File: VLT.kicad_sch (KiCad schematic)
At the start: 65 parts, among them J1 TFT, J2 DEBUG, Q1 AO3401A, Q2 BSS138, Q3 AO3401A, U1 AP2112K-3.3, U2 W25Q128JVS, U3 RP2350B-QFN80, Y1 12MHz

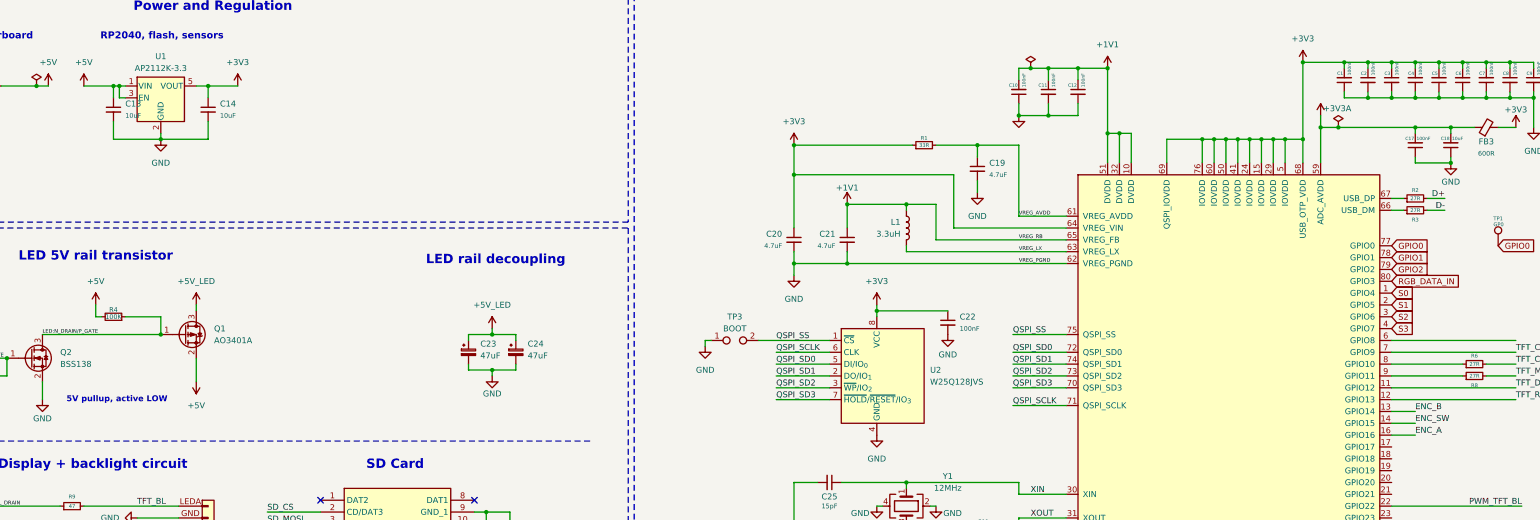
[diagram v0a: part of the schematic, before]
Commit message: Changed encoder pinout A: GP16>GP15, B: GP14>GP15, SW: GP15>GP16
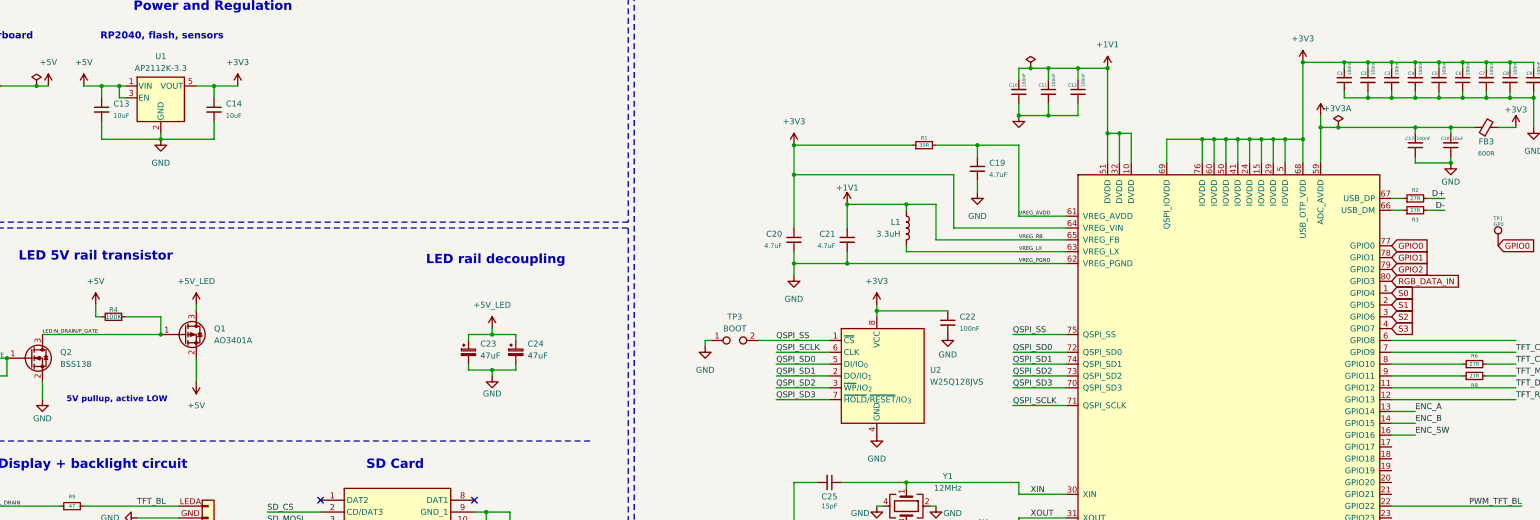
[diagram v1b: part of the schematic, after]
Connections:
- net ENC_A: now also U3.13 (GPIO14); no longer U3.16 (GPIO16)
- net ENC_B: now also U3.14 (GPIO15); no longer U3.13 (GPIO14)
- net ENC_SW: now also U3.16 (GPIO16); no longer U3.14 (GPIO15)
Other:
- moved on the sheet: C13, C14
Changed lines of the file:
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@@
 	)
 	(junction
+		(at 77.47 36.83)
+		(diameter 0)
+		(color 0 0 0 0)
+	)
+	(junction
 		(at 57.15 95.25)
 		(diameter 0)
@@
 	)
 	(junction
-		(at 80.01 36.83)
-		(diameter 0)
-		(color 0 0 0 0)
-	)
-	(junction
 		(at 90.17 48.26)
 		(diameter 0)
@@
 	)
 	(junction
-		(at 384.81 39.37)
+		(at 101.6 36.83)
 		(diameter 0)
 		(color 0 0 0 0)
 	)
 	(junction
-		(at 100.33 36.83)
+		(at 384.81 39.37)
 		(diameter 0)
 		(color 0 0 0 0)
@@
 	(wire
 		(pts
-			(xy 73.66 36.83) (xy 80.01 36.83)
+			(xy 73.66 36.83) (xy 77.47 36.83)
 		)
 		(stroke
@@
 	(wire
 		(pts
+			(xy 77.47 36.83) (xy 81.28 36.83)
+		)
+		(stroke
+			(width 0)
+			(type default)
+		)
+	)
+	(wire
+		(pts
 			(xy 102.87 252.73) (xy 102.87 254)
 		)
@@
 	(wire
 		(pts
-			(xy 100.33 44.45) (xy 100.33 48.26)
+			(xy 101.6 44.45) (xy 101.6 48.26)
 		)
 		(stroke
@@
 	(wire
 		(pts
-			(xy 80.01 44.45) (xy 80.01 48.26)
+			(xy 77.47 44.45) (xy 77.47 48.26)
 		)
 		(stroke
@@
 	(wire
 		(pts
-			(xy 80.01 48.26) (xy 90.17 48.26)
+			(xy 77.47 48.26) (xy 90.17 48.26)
 		)
 		(stroke
@@
 	(wire
 		(pts
-			(xy 97.79 36.83) (xy 100.33 36.83)
+			(xy 97.79 36.83) (xy 101.6 36.83)
 		)
 		(stroke
@@
 	(wire
 		(pts
-			(xy 100.33 48.26) (xy 90.17 48.26)
+			(xy 101.6 48.26) (xy 90.17 48.26)
 		)
 		(stroke
@@
 	(wire
 		(pts
-			(xy 80.01 36.83) (xy 81.28 36.83)
-		)
-		(stroke
-			(width 0)
-			(type default)
-		)
-	)
-	(wire
-		(pts
 			(xy 73.66 127) (xy 93.98 127)
 		)
@@
 	(wire
 		(pts
-			(xy 80.01 39.37) (xy 80.01 36.83)
+			(xy 77.47 39.37) (xy 77.47 36.83)
 		)
 		(stroke
@@
 	(wire
 		(pts
-			(xy 100.33 36.83) (xy 106.68 36.83)
-		)
-		(stroke
-			(width 0)
-			(type default)
-		)
-	)
-	(wire
-		(pts
 			(xy 313.69 48.26) (xy 316.23 48.26)
 		)
@@
 	(wire
 		(pts
-			(xy 100.33 39.37) (xy 100.33 36.83)
+			(xy 101.6 39.37) (xy 101.6 36.83)
 		)
 		(stroke
@@
 	(wire
 		(pts
+			(xy 101.6 36.83) (xy 106.68 36.83)
+		)
+		(stroke
+			(width 0)
+			(type default)
+		)
+	)
+	(wire
+		(pts
 			(xy 85.09 144.78) (xy 93.98 144.78)
 		)
@@
 	)
 	(label "ENC_SW"
-		(at 359.41 109.22 0)
+		(at 359.41 111.76 0)
 		(effects
 			(font
@@
 	)
 	(label "ENC_B"
-		(at 359.41 106.68 0)
+		(at 359.41 109.22 0)
 		(effects
 			(font
@@
 	)
 	(label "ENC_A"
-		(at 359.41 111.76 0)
+		(at 359.41 106.68 0)
 		(effects
 			(font
@@
 	(symbol
 		(lib_id "Mars_Library:Capacitor_0603_10uF")
-		(at 80.01 41.91 0)
+		(at 77.47 41.91 0)
 		(unit 1)
 		(exclude_from_sim no)
@@
 		(fields_autoplaced yes)
 		(property "Reference" "C13"
-			(at 82.55 40.6462 0)
+			(at 80.01 40.6462 0)
 			(effects
 				(font
@@
 		)
 		(property "Value" "10uF"
-			(at 82.55 43.1863 0)
+			(at 80.01 43.1863 0)
 			(effects
 				(font
@@
 		)
 		(property "Footprint" "Mars_Library:C_0603"
-			(at 80.01 41.91 0)
+			(at 77.47 41.91 0)
 			(effects
 				(font
@@
 		)
 		(property "Datasheet" "~"
-			(at 80.01 41.91 0)
+			(at 77.47 41.91 0)
 			(effects
 				(font
@@
 		)
 		(property "Description" "Unpolarized capacitor, small symbol"
-			(at 80.01 41.91 0)
+			(at 77.47 41.91 0)
 			(effects
 				(font
@@
 		)
 		(property "LCSC" "C19702"
-			(at 80.01 41.91 0)
+			(at 77.47 41.91 0)
 			(effects
 				(font
@@
 	(symbol
 		(lib_id "Mars_Library:Capacitor_0603_10uF")
-		(at 100.33 41.91 0)
+		(at 101.6 41.91 0)
 		(unit 1)
 		(exclude_from_sim no)
@@
 		(fields_autoplaced yes)
 		(property "Reference" "C14"
-			(at 102.87 40.6462 0)
+			(at 104.14 40.6462 0)
 			(effects
 				(font
@@
 		)
 		(property "Value" "10uF"
-			(at 102.87 43.1863 0)
+			(at 104.14 43.1863 0)
 			(effects
 				(font
@@
 		)
 		(property "Footprint" "Mars_Library:C_0603"
-			(at 100.33 41.91 0)
+			(at 101.6 41.91 0)
 			(effects
 				(font
@@
 		)
 		(property "Datasheet" "~"
-			(at 100.33 41.91 0)
+			(at 101.6 41.91 0)
 			(effects
 				(font
@@
 		)
 		(property "Description" "Unpolarized capacitor, small symbol"
-			(at 100.33 41.91 0)
+			(at 101.6 41.91 0)
 			(effects
 				(font
@@
 		)
 		(property "LCSC" "C19702"
-			(at 100.33 41.91 0)
+			(at 101.6 41.91 0)
 			(effects
 				(font

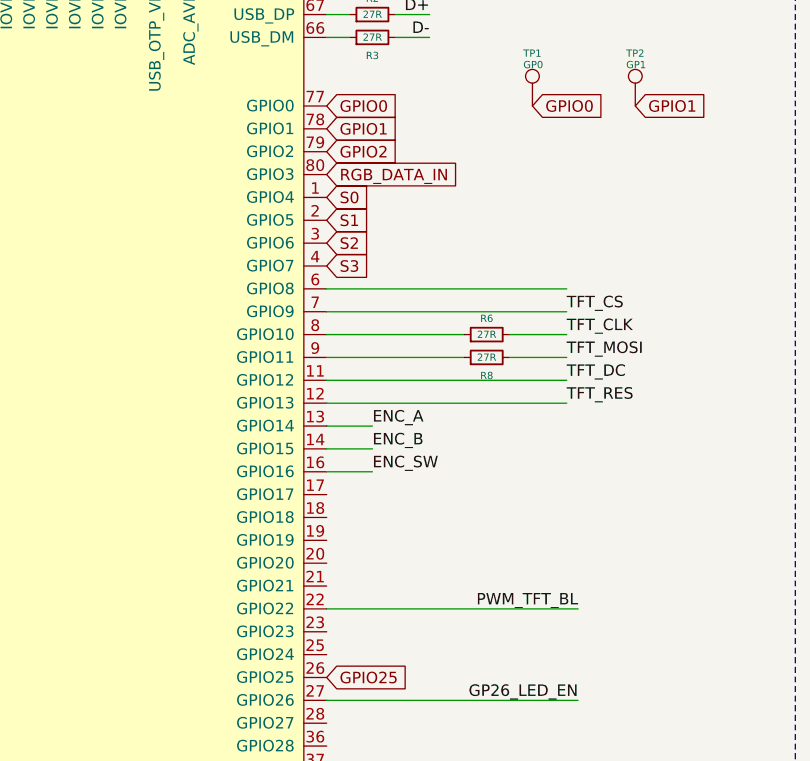
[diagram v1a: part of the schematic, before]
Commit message: Changed WS2812B pin. RGB_DATA_IN: GP3>GP21
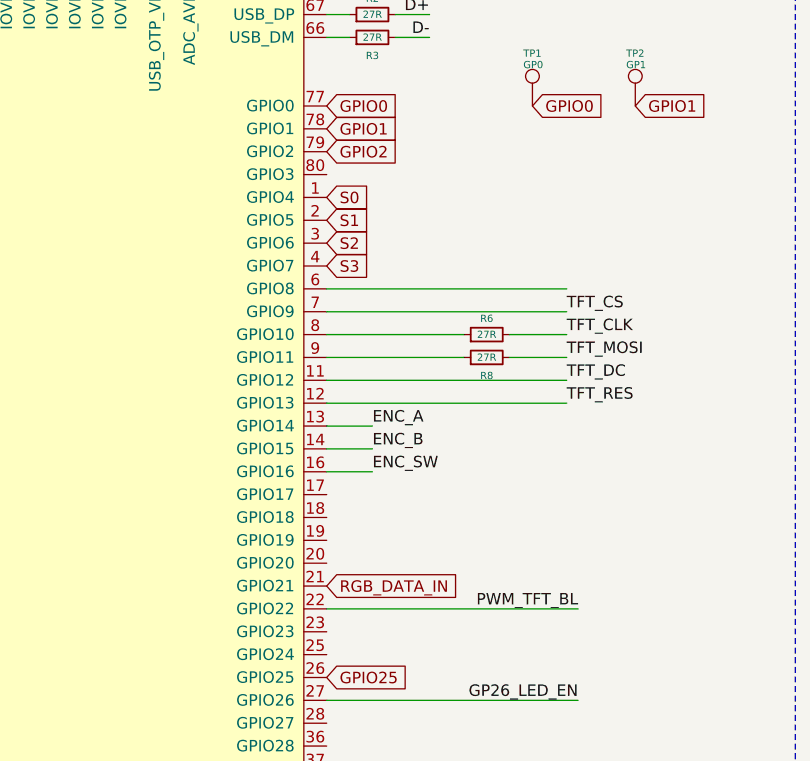
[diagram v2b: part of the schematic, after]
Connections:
- net RGB_DATA_IN: now also U3.21 (GPIO21); no longer U3.80 (GPIO3)
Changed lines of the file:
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@@
+		)
+	)
+	(global_label "RGB_DATA_IN"
+		(shape input)
+		(at 354.33 124.46 0)
+		(fields_autoplaced yes)
+		(effects
+			(font
+				(size 1.27 1.27)
+			)
+			(justify left)
+		)
+		(property "Intersheetrefs" "${INTERSHEET_REFS}"
+			(at 354.33 124.46 0)
+			(effects
+				(font
+					(size 1.27 1.27)
+				)
+				(hide yes)
+			)
 		)
 	)
@@
 				(hide yes)
 			)
-		)
-	)
-	(global_label "RGB_DATA_IN"
-		(shape input)
-		(at 354.33 78.74 0)
-		(fields_autoplaced yes)
-		(effects
-			(font
-				(size 1.27 1.27)
-			)
-			(justify left)
-		)
-		(property "Intersheetrefs" "${INTERSHEET_REFS}"
-			(at 354.33 78.74 0)
-			(effects
-				(font
-					(size 1.27 1.27)
-				)
-				(hide yes)
-			)

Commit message: Remapped pins, added MPR121
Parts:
- added C15, C16: 100nF, Mars_Library:C_0603, symbol Mars_Library:Capacitor_C_0603_100nF_0.1uF
- added R22: 75K, Mars_Library:R_0603, symbol Mars_Library:Resistor_R_0603
- added U4: MPR121QR2, Package_DFN_QFN:UQFN-20_3x3mm_P0.4mm, symbol Sensor_Touch:MPR121QR2
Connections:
- net +3V3: now also C15.1, U4.20 (VDD)
- net GND: now also C15.2, C16.2, R22.2, U4.4 (ADDR), U4.6 (VSS)
- net PWM_TFT_BL: now also U3.48 (GPIO39); no longer U3.22 (GPIO22)
- net MPR_SCL: now reaches U3.23 (GPIO23)
- net MPR_SCL: now also U4.2 (SCL)
- net MPR_IRQ: now reaches U3.25 (GPIO24)
- net MPR_IRQ: now also U4.1 (~{IRQ})
- new net: R22.1, U4.7 (REXT)
- new net: C16.1, U4.5 (VREG)
- new net ELE0: U4.8 (ELE0)
- new net ELE1: U4.9 (ELE1)
- new net ELE10: U4.18 (LED6/ELE10)
- new net ELE11: U4.19 (LED7/ELE11)
- new net ELE2: U4.10 (ELE2)
- new net ELE3: U4.11 (ELE3)
- new net ELE4: U4.12 (LED0/ELE4)
- new net ELE5: U4.13 (LED1/ELE5)
- new net ELE6: U4.14 (LED2/ELE6)
- new net ELE7: U4.15 (LED3/ELE7)
- new net ELE8: U4.16 (LED4/ELE8)
- new net ELE9: U4.17 (LED5/ELE9)
- new net MPR_SDA: U3.22 (GPIO22), U4.3 (SDA)
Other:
- moved on the sheet: ENC2

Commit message: Rev 2: Major PCB rework — haptic motor, MicroSD, NTC, CTP, split spacebar
- Added ERM haptic motor with BSS138 MOSFET driver on GP21
- Added MicroSD card slot (MSD-1-A, push-in/auto-eject)
- Added NTC thermistor with voltage divider
- Added 4-pin 0.5mm FPC connector for capacitive touch panel
- Added ferrite beads (0603 600R, 0805) for power filtering
- Added 1N4148WT protection diode and test point
- Split spacebar support: HE45 alternate 1.75u stabilizer footprint
- Full PCB re-route with 4-layer switch footprints
- All 81 hall sensors relabeled with key names in schematic
- Relaxed DRC (text height, via diameter), new via size 0.6/0.2
- Added CHANGELOG.md and wiring.cpp MUX mapping reference
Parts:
- removed R14: 10K, Mars_Library:R_0402, symbol Mars_Library:R_0603
- removed TP3: BOOT, TestPoint:TestPoint_2Pads_Pitch2.54mm_Drill0.8mm, symbol Connector:TestPoint_2Pole
- added C28: 100nF, Mars_Library:C_0603, symbol Mars_Library:Capacitor_C_0603_100nF_0.1uF
- added D1: 1N4148WT, Diode_SMD:D_SOD-523, symbol Diode:1N4148WT
- added ERM1: Motor_DC, Mars_Library:Coin_Motor_ERM_10mm, symbol Motor:Motor_DC
- added J3: FPC_4P_0.5mm, Mars_Library:XUNPU_FPC-05F-4PH20_1x4-1MP_P0.5mm, symbol Mars_Library:FPC_4P_0.5mm
- added Q4: BSS138, PCM_4ms_Package_SOT:SOT-23, symbol Mars_Transistor:BSS138
- added R14: 10K, Mars_Library:R_0402, symbol Mars_Library:Resistor_R_0402_10K
- added R23, R24: 2.2K, Mars_Library:R_0402, symbol Mars_Library:Resistor_R_0402
- added R25: 1K, Mars_Library:R_0402, symbol Mars_Library:Resistor_R_0402_1K
- added R26, R27, R28, R29: 10K, Mars_Library:R_0603, symbol Mars_Library:Resistor_R_0603_10K
- added SW1: SW_Push_Momentary, Mars_Library:SW_2x3x0.65mm_SPST_Tiny, symbol Mars_Library:SW_Push_Momentary
- added TH1: DNP (10K), Mars_Library:R_0603, symbol Device:Thermistor_NTC
- added TP3: BOOT, Mars_Library:TestPoint_Pad_D1.0mm_Minimal, symbol PCM_4ms_Connector:TestPoint
- J1: footprint Mars_Library:TFT_FPC_8P_0.5mm -> Mars_Library:XUNPU_FPC-05F-8PH20_1x8-1MP_P0.5mm
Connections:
- net +3V3: now also J1.7 (VDD), C28.1, D1.1 (K), ERM1.1 (+), R23.2, R24.2, R26.1, R27.1, R28.1, R29.1; no longer J1.VDD (Pin_7)
- net ELE2: now also J3.1 (Pin_1)
- net ELE4: now also J3.2 (Pin_2)
- net ELE6: now also J3.3 (Pin_3)
- net ELE8: now also J3.4 (Pin_4)
- net ENC_A: now also U3.39 (GPIO31), R26.2; no longer U3.13 (GPIO14)
- net ENC_B: now also U3.38 (GPIO30), R27.2; no longer U3.14 (GPIO15)
- net ENC_SW: now also U3.40 (GPIO32), R28.2; no longer U3.16 (GPIO16)
- net GND: now also J1.2 (GND), C28.2, J3.MP (MountPin), Q4.2 (S), R14.2, SW1.1, TH1.2; no longer J1.GND (Pin_2)
- net MPR_IRQ: now also U3.20 (GPIO20); no longer U3.25 (GPIO24)
- net MPR_SCL: now also U3.19 (GPIO19), R24.1; no longer U3.23 (GPIO23)
- net MPR_SDA: now also U3.18 (GPIO18), R23.1; no longer U3.22 (GPIO22)
- net PWM_TFT_BL: now also U3.22 (GPIO22); no longer U3.48 (GPIO39)
- net QSPI_SS: now also TP3.1
- net RGB_DATA_IN: now also U3.80 (GPIO3); no longer U3.21 (GPIO21)
- net RUN: now also SW1.2
- net TFT_BL: now also J1.1 (LEDA); no longer J1.LEDA (Pin_1)
- net TFT_CLK: now also J1.6 (SCL); no longer J1.SCL (Pin_6)
- net TFT_CS: now also J1.8 (CS); no longer J1.CS (Pin_8)
- net TFT_DC: now also J1.4 (DC); no longer J1.DC (Pin_4)
- net TFT_MOSI: now also J1.5 (SDA); no longer J1.SDA (Pin_5)
- net TFT_RES: now also J1.3 (RES); no longer J1.RES (Pin_3)
- net NTC: now reaches U3.49 (GPIO40_ADC0)
- net NTC: now also R29.2, TH1.1
- new net: Q4.1 (G), R14.1, R25.1
- new net GP21_ERM_GATE: R25.2, U3.21 (GPIO21)
- new net MTR-: D1.2 (A), ERM1.2 (-), Q4.3 (D)
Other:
- moved on the sheet: C15, C16, ENC2, R12, R22, SD1, U4

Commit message: VLT_rev1 PCB complete — production files added
Finalized schematic and PCB layout. Added production/ with
Gerbers (VLT_rev1.zip), BOM, pick-and-place positions, and
IPC netlist for fabrication.
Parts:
- added C29: 100nF, Mars_Library:C_0603, symbol Mars_Library:Capacitor_C_0603_100nF_0.1uF
- added FID3: Fiducial, Fiducial:Fiducial_0.5mm_Mask1mm, symbol Mechanical:Fiducial
- added J5: Conn_01x04_MountingPin, Connector_JST:JST_SH_SM04B-SRSS-TB_1x04-1MP_P1.00mm_Horizontal, symbol Connector_Generic_MountingPin:Conn_01x04_MountingPin
- added TP4: GND, Mars_Library:TestPoint_Pad_D1.0mm_Minimal, symbol PCM_4ms_Connector:TestPoint
- R9: value 47 -> 10R; LCSC (none) -> C22859
- renumbered ENC2 to ENC1
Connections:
- net +3V3: now also C29.1
- net GND: now also C29.2, J5.MP (MountPin), TP4.1
- net GPIO25: now also J5.1 (Pin_1)
- net GPIO14: now reaches U3.13 (GPIO14)
- net GPIO15: now reaches U3.14 (GPIO15)
- net GPIO16: now reaches U3.16 (GPIO16)
- net GPIO17: now reaches U3.17 (GPIO17)
- net GPIO27: now reaches U3.28 (GPIO27)
- net GPIO27: now also J5.3 (Pin_3)
- net GPIO28: now reaches U3.36 (GPIO28)
- net GPIO28: now also J5.4 (Pin_4)
- net GP29_LED_EN: now reaches U3.37 (GPIO29)
- net GP29_LED_EN: now also R5.1
- net GPIO38: now reaches U3.47 (GPIO38)
- net GPIO39: now reaches U3.48 (GPIO39)
- net GP26_LED_EN renamed GPIO26
- net GPIO26: now also J5.2 (Pin_2); no longer R5.1

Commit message: VLT PCB rev: dual TFT connector, RKJXT1F42001 footprint, LED expansion header
- Add 12-pin TFT connector alongside existing 8-pin for CTP-integrated display option
- Superimpose RKJXT1F42001 5-way joystick footprint on EC11 encoder for testing
- Add LED expansion header for additional RGB zones
- Update production files
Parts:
- added C30: 47uF, Capacitor_Tantalum_SMD:CP_EIA-3216-12_Kemet-S, symbol Device:C_Polarized_Small
- added J4: LED_EXP, Connector_JST:JST_GH_SM03B-GHS-TB_1x03-1MP_P1.25mm_Horizontal, symbol Connector_Generic_MountingPin:Conn_01x03_MountingPin
- added J6: TFT, Mars_Library:XUNPU_FPC-05F-12PH20_1x12-1MP_P0.5mm, symbol Mars_Library:Conn_FPC_12P_0.5mm_MP
- added R30, R31, R32, R33: 10K, Mars_Library:R_0402, symbol Mars_Library:Resistor_R_0402_10K
- added S1: RKJXT1F42001, RKJXT1F42001:XDCR_RKJXT1F42001, symbol RKJXT1F42001:RKJXT1F42001
- C25, C26: value 15pF -> 30pF; HQ (none) -> UN0000055
- J5: now not fitted
- U3: HQ (none) -> IC138557869
- Y1: HQ (none) -> CR0250572
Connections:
- net +3V3: now also C30.1, J6.4 (VDD), R30.1, R31.1, R32.1, R33.1
- net +5V_LED: now also J4.1 (Pin_1)
- net ENC_A: now also S1.EN_A
- net ENC_B: now also S1.EN_B
- net ENC_SW: now also S1.P (PUSH)
- net GND: now also C30.2, J4.3 (Pin_3), J4.MP (MountPin), J6.1 (PWR_GND), J6.12 (PWR_GND), J6.2 (LEDK_Cathode), J6.5 (PWR_GND), J6.6 (PWR_GND), J6.MP (MountPin), S1.COM, S1.EN_COM, S1.GND
- net GPIO14: now also R30.2, S1.A
- net GPIO15: now also R31.2, S1.B
- net GPIO16: now also R32.2, S1.C
- net GPIO17: now also R33.2, S1.D
- net PWM_TFT_BL: now also U3.6 (GPIO8); no longer U3.22 (GPIO22)
- net TFT_BL: now also J6.3 (LEDA_Anode)
- net TFT_CLK: now also J6.9 (SCL)
- net TFT_CS: now also J6.8 (CS)
- net TFT_DC: now also J6.7 (DC)
- net TFT_MOSI: now also J6.10 (SDA)
- net TFT_RES: now also J6.11 (RESET)
- new net LED_EXP: J4.2 (Pin_2)
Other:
- moved on the sheet: C15, C16, C28, D1, ENC1, ERM1, J3, Q4, R12, R14, R22, R23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
